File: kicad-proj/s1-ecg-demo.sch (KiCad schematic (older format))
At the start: 42 parts, among them J1 USB-C-16-Pin, J2 Conn_ARM_JTAG_SWD_10, J3 Battery Port, J4 Current Probe, U1 AD8233

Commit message: updated to match eval board
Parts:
- added R23: 100k, symbol Device:R_Small
- C2: value 12n -> 10n
- C7: value 0.1u -> 1u
- R10: value 10M -> 499k
- R12, R13: value 150k -> 182k
- R5: value 150k -> 200k
- U1: footprint (none) -> s1-ecg-demo:WLCSP-20
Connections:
- net +3V3: now also U1.B3 (FR)
- net GND: no longer U1.B3 (FR)
- net LED7: now also MOD1.6 (D7); no longer MOD1.7 (D8)
- net LOD: now also MOD1.15 (A2); no longer MOD1.6 (D7)
- net RA: no longer MOD1.15 (A2)
- net at C4.1, R4.2, R8.1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: now also R23.1
- net at C3.2, U1.C4 (RLDFB): no longer R10.1
- net at U1.D4 (SW): now also R23.2
- net at C3.1, R6.2, R7.2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: now also R10.1; no longer R10.2
- new net RL: R10.2
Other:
- moved on the sheet: R6, R7
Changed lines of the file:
@@
 F 0 "U1" H 8825 5115 50  0000 C CNN
 F 1 "AD8233" H 8825 5024 50  0000 C CNN
-F 2 "" H 7575 2950 50  0001 C CNN
-F 3 "" H 7575 2950 50  0001 C CNN
+F 2 "s1-ecg-demo:WLCSP-20" H 7575 2950 50  0001 C CNN
+F 3 "https://www.analog.com/media/en/technical-documentation/data-sheets/ad8233.pdf" H 7575 2950 50  0001 C CNN
 	1    8825 3450
 	1    0    0    -1
@@
 P 10250 3025
 F 0 "C7" H 10342 3071 50  0000 L CNN
-F 1 "0.1u" H 10342 2980 50  0000 L CNN
+F 1 "1u" H 10342 2980 50  0000 L CNN
 F 2 "" H 10250 3025 50  0001 C CNN
 F 3 "~" H 10250 3025 50  0001 C CNN
@@
 P 7300 4625
 F 0 "C2" H 7575 4550 50  0000 R CNN
-F 1 "12n" H 7575 4650 50  0000 R CNN
+F 1 "10n" H 7575 4650 50  0000 R CNN
 F 2 "" H 7300 4625 50  0001 C CNN
 F 3 "~" H 7300 4625 50  0001 C CNN
@@
 	9625 4250 9425 4250
 $Comp
-L Device:R_Small R10
-U 1 1 611962E1
-P 7725 3150
-F 0 "R10" H 7775 3175 50  0000 L CNN
-F 1 "10M" H 7775 3100 50  0000 L CNN
-F 2 "" H 7725 3150 50  0001 C CNN
-F 3 "~" H 7725 3150 50  0001 C CNN
-	1    7725 3150
-	1    0    0    -1
-$EndComp
-$Comp
 L Device:R_Small R7
 U 1 1 61197DAA
-P 7475 2925
-F 0 "R7" H 7550 3000 50  0000 L CNN
-F 1 "10M" H 7550 2925 50  0000 L CNN
-F 2 "" H 7475 2925 50  0001 C CNN
-F 3 "~" H 7475 2925 50  0001 C CNN
-	1    7475 2925
-	1    0    0    -1
-$EndComp
-Wire Wire Line
-	7725 3050 7725 3000
-Wire Wire Line
-	7725 3000 8050 3000
-Connection ~ 8050 3000
-Wire Wire Line
-	7725 3250 7725 3300
-Wire Wire Line
-	7725 3300 8050 3300
+P 7700 2925
+F 0 "R7" H 7775 3000 50  0000 L CNN
+F 1 "10M" H 7775 2925 50  0000 L CNN
+F 2 "" H 7700 2925 50  0001 C CNN
+F 3 "~" H 7700 2925 50  0001 C CNN
+	1    7700 2925
+	1    0    0    -1
+$EndComp
 Connection ~ 8050 3300
 Wire Wire Line
-	7725 3300 7475 3300
-Wire Wire Line
-	7475 3300 7475 3025
-Connection ~ 7725 3300
+	7700 3300 7700 3025
 $Comp
 L Device:R_Small R6
 U 1 1 6119C8AC
-P 7200 3100
-F 0 "R6" H 7025 3125 50  0000 L CNN
-F 1 "10M" H 7000 3025 50  0000 L CNN
-F 2 "" H 7200 3100 50  0001 C CNN
-F 3 "~" H 7200 3100 50  0001 C CNN
-	1    7200 3100
-	1    0    0    -1
-$EndComp
-Wire Wire Line
-	7200 3200 7200 3300
-Wire Wire Line
-	7200 3300 7475 3300
-Connection ~ 7475 3300
+P 7525 3100
+F 0 "R6" H 7350 3125 50  0000 L CNN
+F 1 "10M" H 7325 3025 50  0000 L CNN
+F 2 "" H 7525 3100 50  0001 C CNN
+F 3 "~" H 7525 3100 50  0001 C CNN
+	1    7525 3100
+	1    0    0    -1
+$EndComp
+Wire Wire Line
+	7525 3200 7525 3300
+Wire Wire Line
+	7525 3300 7700 3300
+Connection ~ 7700 3300
 $Comp
 L Device:R_Small R12
@@
 P 7925 2400
 F 0 "R12" V 7750 2325 50  0000 L CNN
-F 1 "150k" V 7825 2325 50  0000 L CNN
+F 1 "182k" V 7825 2325 50  0000 L CNN
 F 2 "" H 7925 2400 50  0001 C CNN
 F 3 "~" H 7925 2400 50  0001 C CNN
@@
 P 7925 2700
 F 0 "R13" V 7750 2625 50  0000 L CNN
-F 1 "150k" V 7825 2625 50  0000 L CNN
+F 1 "182k" V 7825 2625 50  0000 L CNN
 F 2 "" H 7925 2700 50  0001 C CNN
 F 3 "~" H 7925 2700 50  0001 C CNN
@@
 	8025 2400 8225 2400
 Wire Wire Line
-	7825 2700 7200 2700
-Wire Wire Line
-	7825 2400 7475 2400
-Wire Wire Line
-	7475 2825 7475 2400
-Connection ~ 7475 2400
-Wire Wire Line
-	7475 2400 6550 2400
-Wire Wire Line
-	7200 3000 7200 2700
-Connection ~ 7200 2700
-NoConn ~ 8225 3600
+	7825 2700 7525 2700
+Wire Wire Line
+	7825 2400 7700 2400
+Wire Wire Line
+	7700 2825 7700 2400
+Connection ~ 7700 2400
+Wire Wire Line
+	7700 2400 6550 2400
+Wire Wire Line
+	7525 3000 7525 2700
+Connection ~ 7525 2700
 $Comp
 L Device:R_Small R5
@@
 P 7125 3900
 F 0 "R5" V 7275 3875 50  0000 L CNN
-F 1 "150k" V 7200 3800 50  0000 L CNN
+F 1 "200k" V 7200 3800 50  0000 L CNN
 F 2 "" H 7125 3900 50  0001 C CNN
 F 3 "~" H 7125 3900 50  0001 C CNN
@@
 Connection ~ 6925 3900
 Wire Wire Line
-	7200 2700 6550 2700
+	7525 2700 6550 2700
 NoConn ~ 3175 2750
 Wire Wire Line
@@
 	10250 3300 10475 3300
 Connection ~ 10250 3300
-Wire Wire Line
-	9625 3900 9825 3900
-Connection ~ 9625 3900
 Text Label 6550 2700 2    50   ~ 0
 RA
@@
 	3175 2450 3450 2450
 Text Label 3450 2450 0    50   ~ 0
-RA
+LOD
 Wire Wire Line
 	3175 2350 3450 2350
@@
 LED1
 Text Label 1900 2450 2    50   ~ 0
-LOD
+LED7
 Text Label 1900 2650 2    50   ~ 0
 LED6
@@
 Wire Wire Line
 	2175 2750 1900 2750
-Text Label 1900 2550 2    50   ~ 0
-LED7
 Wire Wire Line
 	1900 2550 2175 2550
@@
 $EndComp
 $Comp
-L power:GND #PWR04
-U 1 1 612A9D4F
-P 9625 3600
-F 0 "#PWR04" H 9625 3350 50  0001 C CNN
-F 1 "GND" H 9700 3650 50  0001 C CNN
-F 2 "" H 9625 3600 50  0001 C CNN
-F 3 "" H 9625 3600 50  0001 C CNN
-	1    9625 3600
-	1    0    0    -1
-$EndComp
-$Comp
 L power:GND #PWR06
 U 1 1 612AC006
@@
 L power:+3V3 #PWR05
 U 1 1 612C0F0A
-P 9825 3900
-F 0 "#PWR05" H 9825 3750 50  0001 C CNN
-F 1 "+3V3" H 9725 4050 50  0000 L CNN
-F 2 "" H 9825 3900 50  0001 C CNN
-F 3 "" H 9825 3900 50  0001 C CNN
-	1    9825 3900
+P 9800 3600
+F 0 "#PWR05" H 9800 3450 50  0001 C CNN
+F 1 "+3V3" H 9700 3750 50  0000 L CNN
+F 2 "" H 9800 3600 50  0001 C CNN
+F 3 "" H 9800 3600 50  0001 C CNN
+	1    9800 3600
 	1    0    0    -1
 $EndComp
@@
 $EndComp
 $Comp
-L power:GND #PWR?
+L power:GND #PWR08
 U 1 1 612FCD59
 P 1900 1950
-F 0 "#PWR?" H 1900 1700 50  0001 C CNN
+F 0 "#PWR08" H 1900 1700 50  0001 C CNN
 F 1 "GND" H 1975 2000 50  0001 C CNN
 F 2 "" H 1900 1950 50  0001 C CNN
@@
 $EndComp
 $Comp
-L power:+3V3 #PWR?
+L power:+3V3 #PWR012
 U 1 1 612FFD06
 P 9775 2650
-F 0 "#PWR?" H 9775 2500 50  0001 C CNN
+F 0 "#PWR012" H 9775 2500 50  0001 C CNN
 F 1 "+3V3" H 9675 2800 50  0000 L CNN
 F 2 "" H 9775 2650 50  0001 C CNN
@@
 $EndComp
 $Comp
-L power:GND #PWR?
+L power:GND #PWR011
 U 1 1 61352A98
 P 3825 7375
-F 0 "#PWR?" H 3825 7125 50  0001 C CNN
+F 0 "#PWR011" H 3825 7125 50  0001 C CNN
 F 1 "GND" H 3900 7425 50  0001 C CNN
 F 2 "" H 3825 7375 50  0001 C CNN
@@
 $EndComp
 $Comp
-L power:GND #PWR?
+L power:GND #PWR07
 U 1 1 61355C6C
 P 1475 7375
-F 0 "#PWR?" H 1475 7125 50  0001 C CNN
+F 0 "#PWR07" H 1475 7125 50  0001 C CNN
 F 1 "GND" H 1550 7425 50  0001 C CNN
 F 2 "" H 1475 7375 50  0001 C CNN
@@
 $EndComp
 $Comp
-L power:GND #PWR?
+L power:GND #PWR09
 U 1 1 61356705
 P 2575 6175
-F 0 "#PWR?" H 2575 5925 50  0001 C CNN
+F 0 "#PWR09" H 2575 5925 50  0001 C CNN
 F 1 "GND" H 2650 6225 50  0001 C CNN
 F 2 "" H 2575 6175 50  0001 C CNN
@@
 $EndComp
 $Comp
-L power:GND #PWR?
+L power:GND #PWR010
 U 1 1 61359CD0
 P 3450 1950
-F 0 "#PWR?" H 3450 1700 50  0001 C CNN
+F 0 "#PWR010" H 3450 1700 50  0001 C CNN
 F 1 "GND" H 3525 2000 50  0001 C CNN
 F 2 "" H 3450 1950 50  0001 C CNN
@@
 $EndComp
 $Comp
-L power:GND #PWR?
+L power:GND #PWR04
 U 1 1 6135CB63
 P 1350 5075
-F 0 "#PWR?" H 1350 4825 50  0001 C CNN
+F 0 "#PWR04" H 1350 4825 50  0001 C CNN
 F 1 "GND" H 1425 5125 50  0001 C CNN
 F 2 "" H 1350 5075 50  0001 C CNN
@@
 	1    0    0    -1
 $EndComp
+Wire Wire Line
+	7700 3300 8050 3300
+$Comp
+L Device:R_Small R10
+U 1 1 611989CB
+P 7150 3300
+F 0 "R10" V 6950 3225 50  0000 L CNN
+F 1 "499k" V 7025 3225 50  0000 L CNN
+F 2 "" H 7150 3300 50  0001 C CNN
+F 3 "~" H 7150 3300 50  0001 C CNN
+	1    7150 3300
+	0    1    1    0
+$EndComp
+Wire Wire Line
+	7250 3300 7525 3300
+Connection ~ 7525 3300
+Wire Wire Line
+	7050 3300 6550 3300
+Text Label 6550 3300 2    50   ~ 0
+RL
+NoConn ~ 1900 2550
+$Comp
+L Device:R_Small R23
+U 1 1 611B2E24
+P 7975 3600
+F 0 "R23" V 8125 3575 50  0000 L CNN
+F 1 "100k" V 8050 3500 50  0000 L CNN
+F 2 "" H 7975 3600 50  0001 C CNN
+F 3 "~" H 7975 3600 50  0001 C CNN
+	1    7975 3600
+	0    -1   -1   0
+$EndComp
+Wire Wire Line
+	8075 3600 8225 3600
+Wire Wire Line
+	7625 4250 7625 3600
+Wire Wire Line
+	7625 3600 7875 3600
+Wire Wire Line
+	9625 3900 9625 3600
+Connection ~ 9625 3900
+Wire Wire Line
+	9800 3600 9625 3600
+Connection ~ 9625 3600
 $EndSCHEMATC

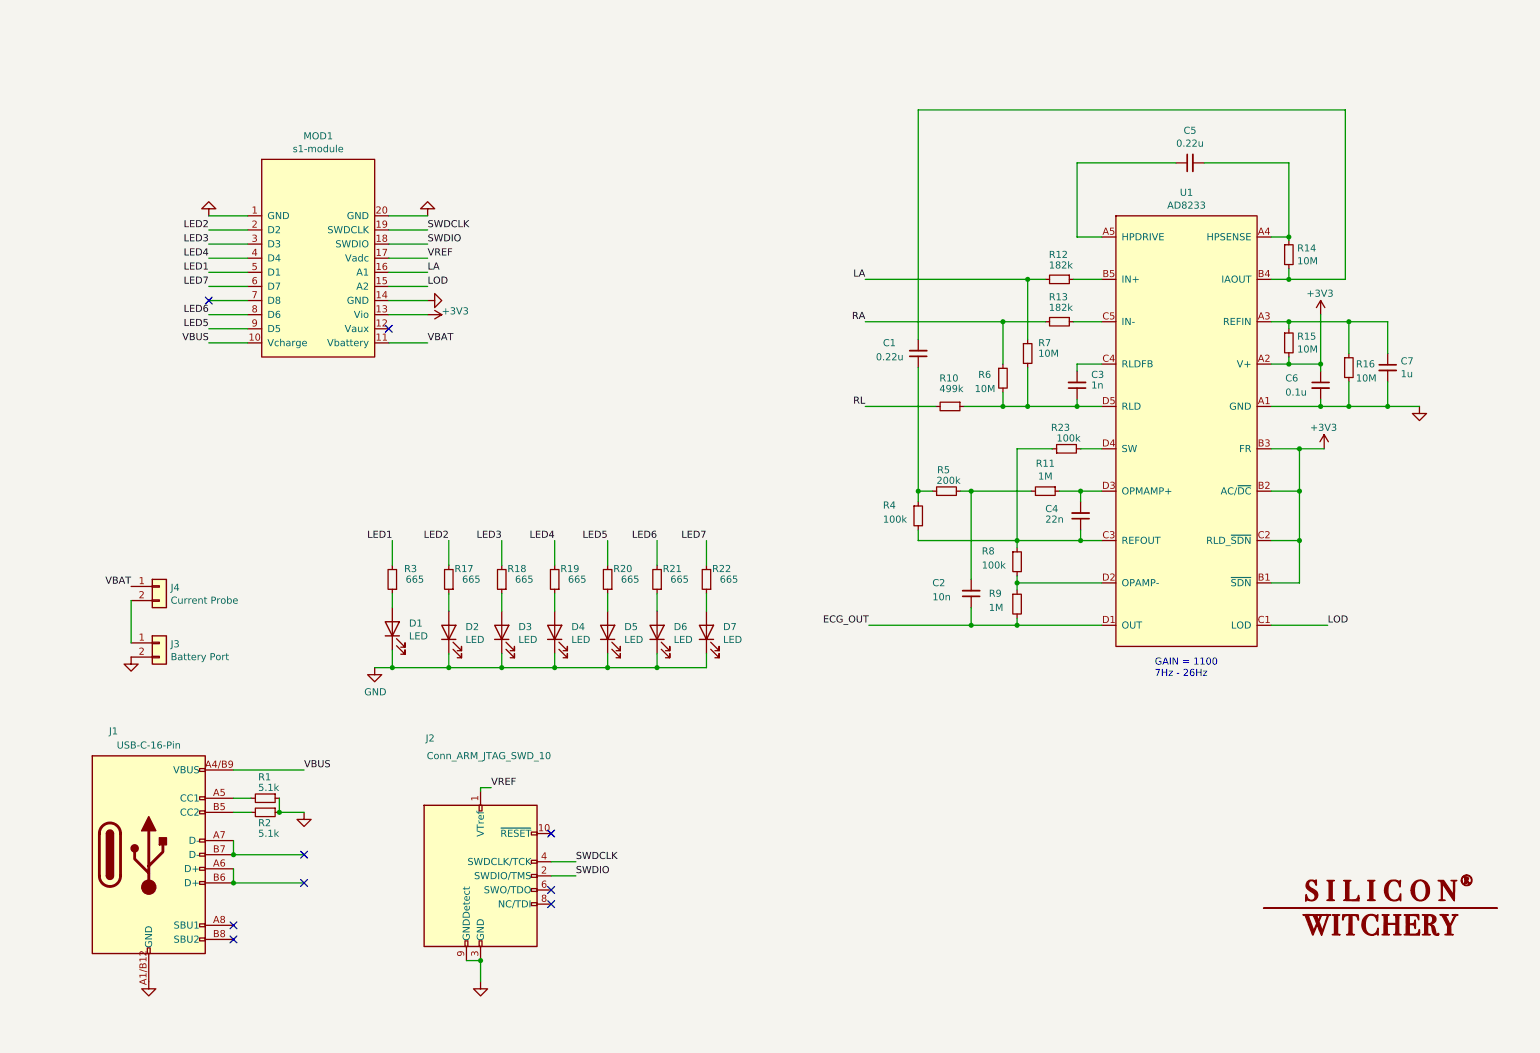
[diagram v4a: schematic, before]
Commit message: pill shape, nearly done routing
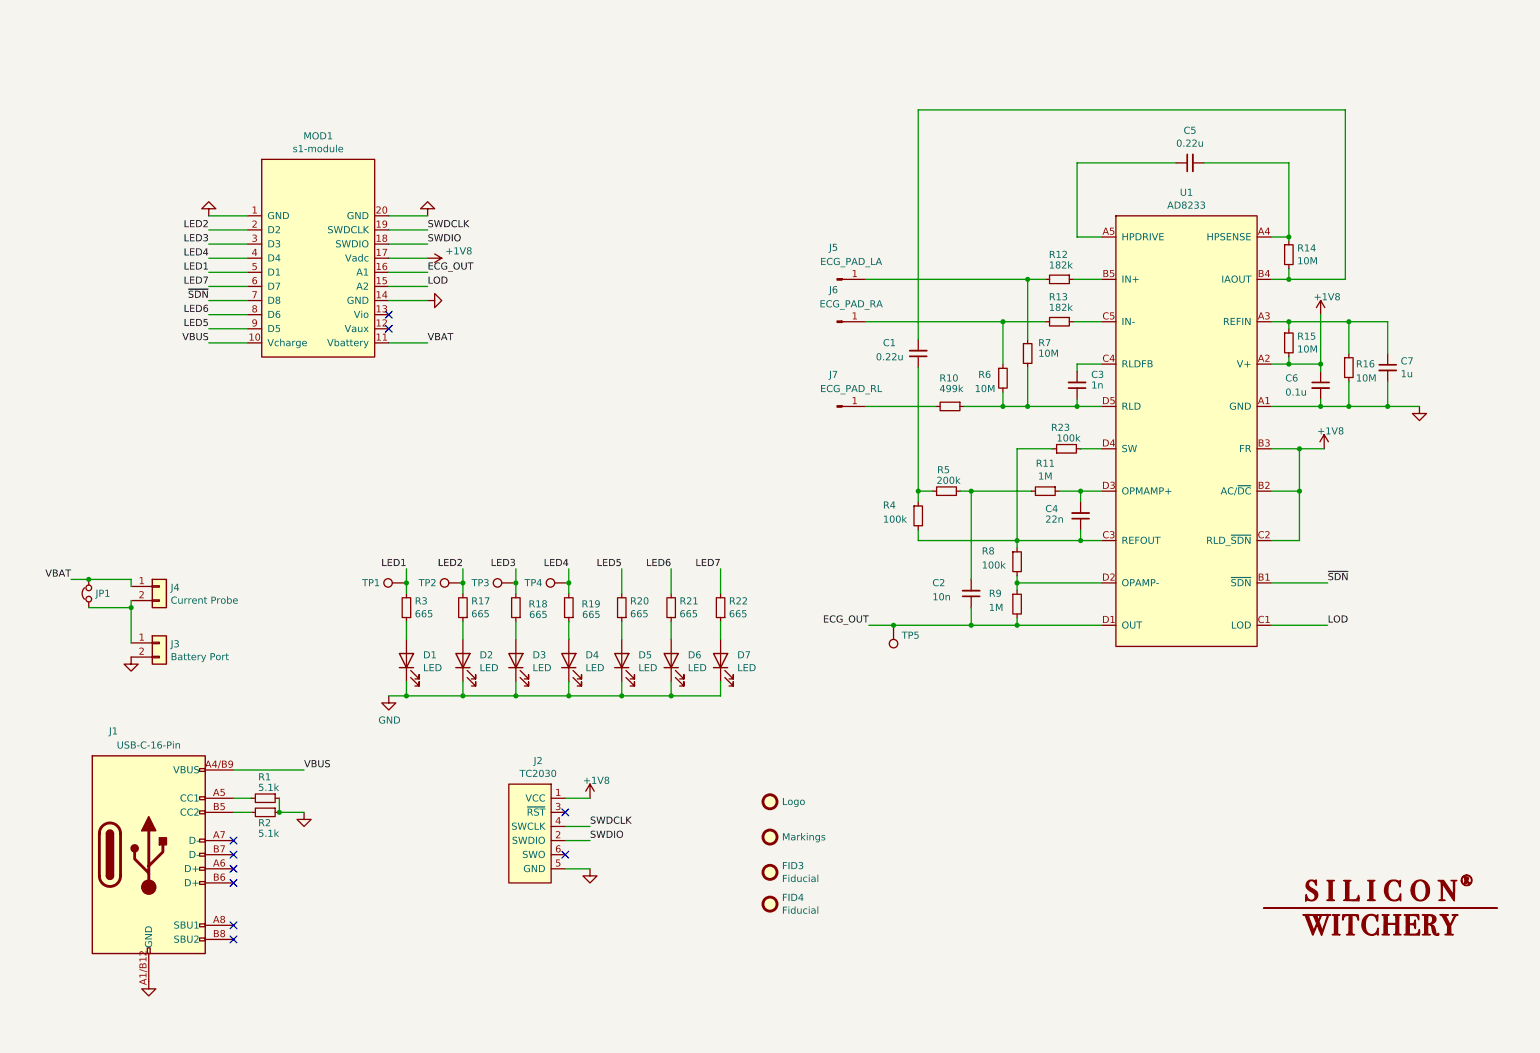
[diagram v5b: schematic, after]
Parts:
- removed J2: Conn_ARM_JTAG_SWD_10, symbol Connector:Conn_ARM_JTAG_SWD_10
- added FID1: Logo, symbol Mechanical:Fiducial
- added FID2: Markings, symbol Mechanical:Fiducial
- added FID3, FID4: Fiducial, Fiducial:Fiducial_0.5mm_Mask1mm, symbol Mechanical:Fiducial
- added J2: TC2030, Connector:Tag-Connect_TC2030-IDC-NL_2x03_P1.27mm_Vertical, symbol s1-ecg-demo:TC2030
- added J5: ECG_PAD_LA, s1-ecg-demo:ECG-pad, symbol Connector:Conn_01x01_Male
- added J6: ECG_PAD_RA, s1-ecg-demo:ECG-pad, symbol Connector:Conn_01x01_Male
- added J7: ECG_PAD_RL, s1-ecg-demo:ECG-pad, symbol Connector:Conn_01x01_Male
- added JP1: Jumper_NC_Small, Jumper:SolderJumper-2_P1.3mm_Bridged_RoundedPad1.0x1.5mm, symbol Device:Jumper_NC_Small
- added TP1, TP2, TP3, TP4, TP5: Tp, TestPoint:TestPoint_Pad_1.0x1.0mm, symbol Connector:TestPoint
- C1, C2, C3, C4, C5, C6, C7: footprint (none) -> Capacitor_SMD:C_0402_1005Metric
- D1, D2, D3, D4, D5, D6, D7: footprint (none) -> LED_SMD:LED_0603_1608Metric
- J1: footprint (none) -> s1-ecg-demo:DX07S016JA1R1500
- J3, J4: footprint (none) -> s1-ecg-demo:Conn_2_SMD_2.54mm
- R1, R10, R11, R12, R13, R14, R15, R16, R17, R18, R19, R2, R20, R21, R22, R23, R3, R4, R5, R6, R7, R8, R9: footprint (none) -> Resistor_SMD:R_0201_0603Metric
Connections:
- net VREF is gone; now on net +1V8: MOD1.17 (Vadc)
- net ECG_OUT: now also MOD1.16 (A1), TP5.1
- net GND: now also J2.5 (GND)
- net LED1: now also TP1.1
- net LED2: now also TP2.1
- net LED3: now also TP3.1
- net LED4: now also TP4.1
- net SWDCLK: now also J2.4 (SWCLK)
- net SWDIO: now also J2.2 (SWDIO)
- net VBAT: now also JP1.2
- net ~SDN: now reaches MOD1.7 (D8)
- net ~SDN: now also U1.B1 (~SDN)
- net at J1.A6 (D+): no longer J1.B6 (D+)
- net at J1.A7 (D-): no longer J1.B7 (D-)
- net at J3.1 (Pin_1), J4.2 (Pin_2): now also JP1.1
- net +3V3 renamed +1V8
- net +1V8: now also J2.1 (VCC); no longer MOD1.13 (Vio), U1.B1 (~SDN)
- net LA: no longer names the net of R12.2, R7.1
- net LA: now also J5.1 (Pin_1); no longer MOD1.16 (A1)
- net RA: no longer names the net of R13.2, R6.1
- net RA: now also J6.1 (Pin_1)
- net RL: no longer names the net of R10.2
- net RL: now also J7.1 (Pin_1)
- no-connect marks 9 -> 10
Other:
- note removed: "GAIN = 1100\n7Hz - 26Hz"
- moved on the sheet: D1, D2, D3, D4, D5, D6, D7, R17, R18, R19, R20, R21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

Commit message: Layout complete, needs checking
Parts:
- added FID3: Heartbeat icon, s1-ecg-demo:heartbeat, symbol Mechanical:Fiducial
- FID1: footprint (none) -> s1-ecg-demo:sw-logo
- FID2: value Markings -> Board title; footprint (none) -> s1-ecg-demo:title
- J1: renamed from J5; value ECG_PAD_LA -> Left arm
- J2: renamed from J6; value ECG_PAD_RA -> Right arm
- J3: renamed from J7; value ECG_PAD_RL -> Right leg
- TP1: renamed from TP5; value Tp -> ECG out; footprint TestPoint:TestPoint_Pad_1.0x1.0mm -> TestPoint:TestPoint_Pad_D1.0mm
- TP2: renamed from TP1; value Tp -> D1; footprint TestPoint:TestPoint_Pad_1.0x1.0mm -> TestPoint:TestPoint_Pad_D1.0mm
- TP3: renamed from TP2; value Tp -> D2; footprint TestPoint:TestPoint_Pad_1.0x1.0mm -> TestPoint:TestPoint_Pad_D1.0mm
- TP4: renamed from TP3; value Tp -> D3; footprint TestPoint:TestPoint_Pad_1.0x1.0mm -> TestPoint:TestPoint_Pad_D1.0mm
- TP5: renamed from TP4; value Tp -> D4; footprint TestPoint:TestPoint_Pad_1.0x1.0mm -> TestPoint:TestPoint_Pad_D1.0mm
- renumbered FID3 to FID4, FID4 to FID5, J1 to J4, J2 to J5, J4 to J6, J3 to J7, D1 to LED1, D2 to LED2, D3 to LED3, D4 to LED4, D5 to LED5, D6 to LED6, D7 to LED7, R4 to R1, R11 to R10, R12 to R11, R13 to R12, R23 to R13, R18 to R14, R19 to R15, R20 to R16, R21 to R17, R14 to R18, R15 to R19, R5 to R2, R22 to R20, R16 to R21, R1 to R22, R2 to R23, R10 to R3, R3 to R4, R6 to R5, R17 to R6, R8 to R7, R9 to R8, R7 to R9
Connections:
- net SWDCLK: no longer names the net of J5.4 (SWCLK), MOD1.19 (SWDCLK)
- net SWDIO: no longer names the net of J5.2 (SWDIO), MOD1.18 (SWDIO)
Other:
- note added: "Battery header &\ncurrent sense"
- note added: "ECG frontend"
- note added: "Pulse LEDs"
- note added: "S1 module &\nprogramming port"
- note added: "USB-C charge port"
- moved on the sheet: C1, C2, C3, C4, C5, C6, C7, FID4, FID5, J1, J2, J3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
